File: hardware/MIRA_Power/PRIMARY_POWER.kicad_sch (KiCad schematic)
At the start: 0 parts

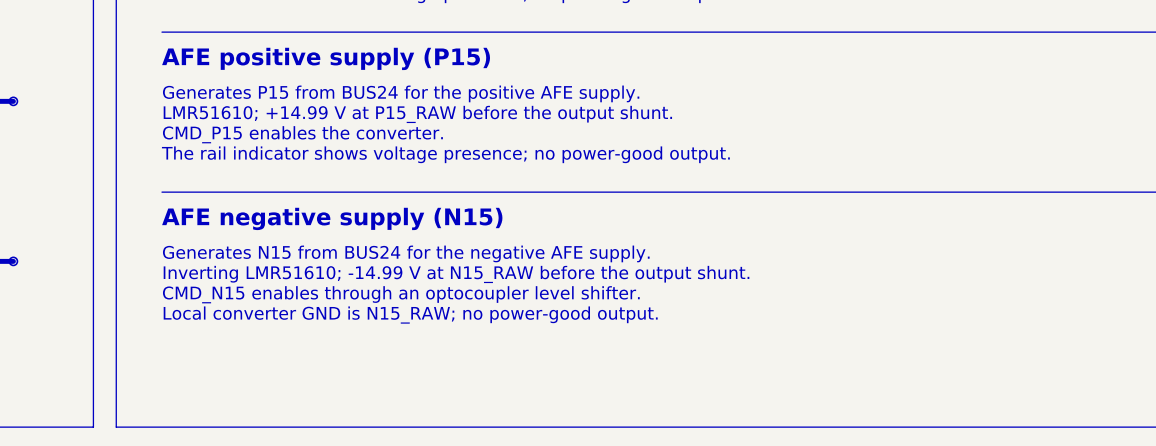
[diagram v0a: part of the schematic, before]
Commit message: Add high-load schematic candidate with CORE sense and revised N15 supply
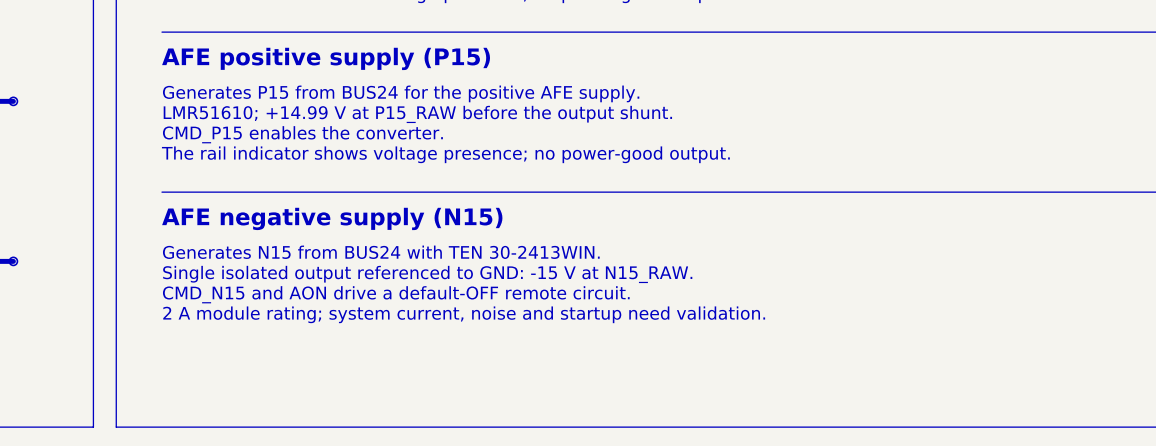
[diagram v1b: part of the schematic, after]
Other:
- note added: "Generates N15 from BUS24 with TEN 30-2413WIN. Single isolated output referenced to GND: -15 V at N15_RAW. CMD_N15 and AON drive a default-OFF remote circuit. 2 A module rating; system current, noise and startup need validation."
- note removed: "Generates N15 from BUS24 for the negative AFE supply. Inverting LMR51610; -14.99 V at N15_RAW before the output shunt. CMD_N15 enables through an optocoupler level shifter. Local converter GND is N15_RAW; no power-good output."
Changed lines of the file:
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@@
 		)
 	)
-	(text "Generates N15 from BUS24 for the negative AFE supply.\nInverting LMR51610; -14.99 V at N15_RAW before the output shunt.\nCMD_N15 enables through an optocoupler level shifter.\nLocal converter GND is N15_RAW; no power-good output."
+	(text "Generates N15 from BUS24 with TEN 30-2413WIN.\nSingle isolated output referenced to GND: -15 V at N15_RAW.\nCMD_N15 and AON drive a default-OFF remote circuit.\n2 A module rating; system current, noise and startup need validation."
 		(exclude_from_sim no)
 		(at 156.21 141.36 0)
